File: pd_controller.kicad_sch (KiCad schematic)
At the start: 29 parts, among them Q1 IRF9358TRPBF, Q2 BSL308PEH6327XTSA1, Q3 NVTR4503NT1G, U1 CYPD3177-24LQXQT

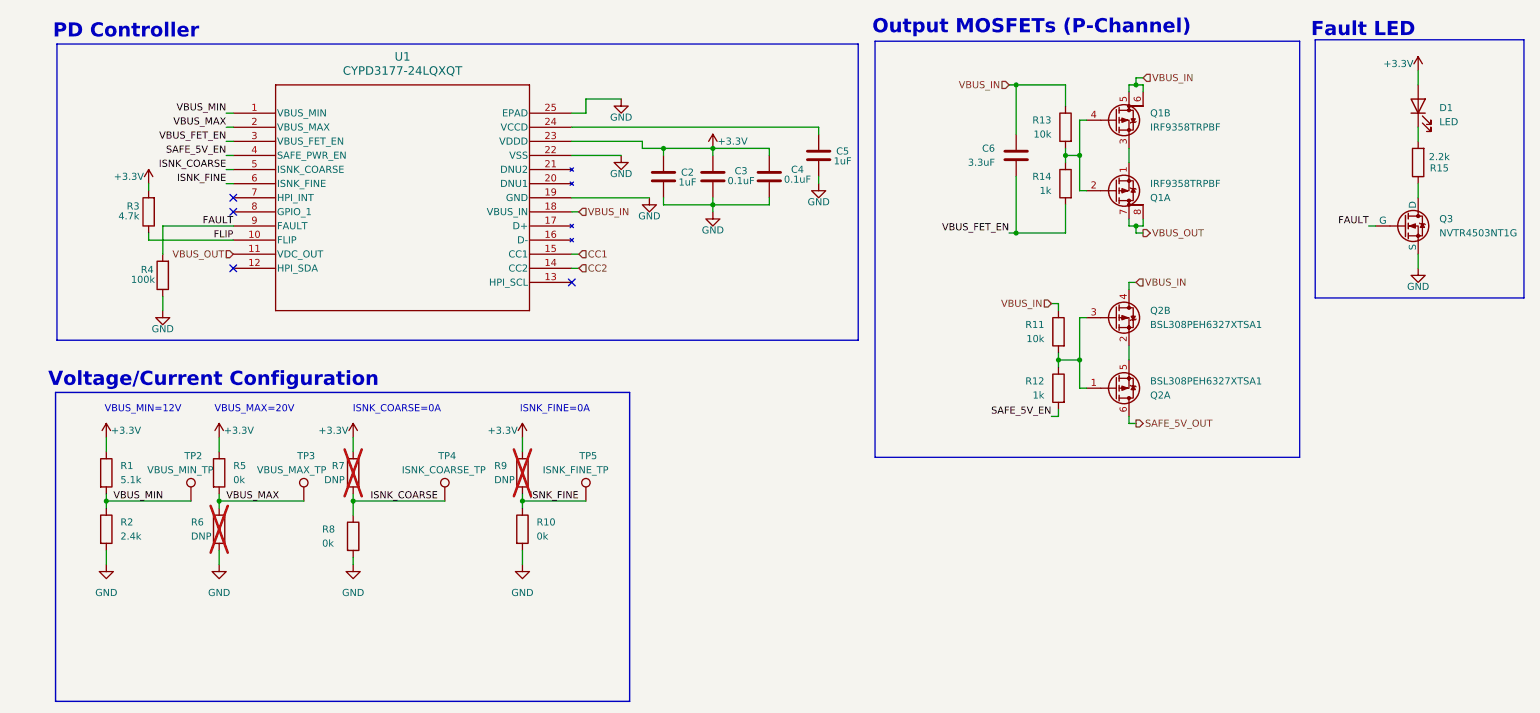
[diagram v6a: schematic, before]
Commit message: cleaned up schematic, added power LEDs and testpoints
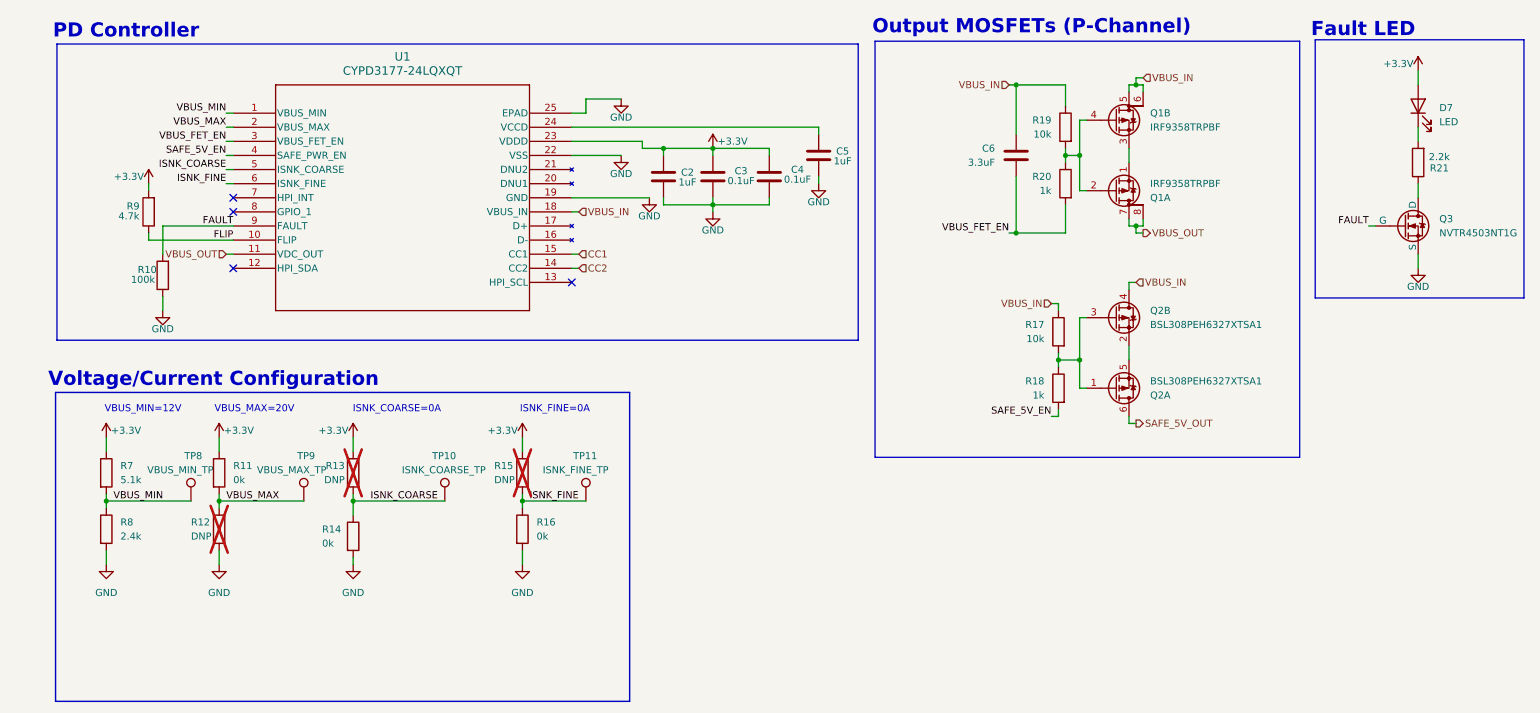
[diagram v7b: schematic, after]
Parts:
- D7: renamed from D1; If (none) -> 2mA; Vf (none) -> 1.9V
- renumbered R4 to R10, R5 to R11, R6 to R12, R7 to R13, R8 to R14, R9 to R15, R10 to R16, R11 to R17, R12 to R18, R13 to R19, R14 to R20, R15 to R21, R1 to R7, R2 to R8, R3 to R9, TP4 to TP10, TP5 to TP11, TP2 to TP8, TP3 to TP9

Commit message: finished footprint assignment
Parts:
- Q1: footprint (none) -> UTSVT_ICs:SO8_IRF9358TRPBF_INF
- Q2: footprint (none) -> Package_TO_SOT_SMD:SOT-23-6
- Q3: footprint (none) -> Package_TO_SOT_SMD:SOT-23-3
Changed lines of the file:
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@@
 			)
 		)
-		(property "Footprint" ""
+		(property "Footprint" "Package_TO_SOT_SMD:SOT-23-6"
 			(at 210.82 105.41 0)
 			(effects
@@
 			)
 		)
-		(property "Footprint" ""
+		(property "Footprint" "Package_TO_SOT_SMD:SOT-23-6"
 			(at 210.82 92.71 0)
 			(effects
@@
 			)
 		)
-		(property "Footprint" ""
+		(property "Footprint" "Package_TO_SOT_SMD:SOT-23-3"
 			(at 266.7 73.66 0)
 			(effects
@@
 			)
 		)
-		(property "Footprint" ""
+		(property "Footprint" "UTSVT_ICs:SO8_IRF9358TRPBF_INF"
 			(at 210.82 57.15 0)
 			(effects
@@
 			)
 		)
-		(property "Footprint" ""
+		(property "Footprint" "UTSVT_ICs:SO8_IRF9358TRPBF_INF"
 			(at 210.82 69.85 0)
 			(effects
